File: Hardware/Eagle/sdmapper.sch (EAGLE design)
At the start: 30 parts, among them IC1 AM29F010J, IC2 HM628512ASOP32, IC3 XC95144XL_TQ100, IC4 LM1117-3V3, T1 BC857, T2 BC857

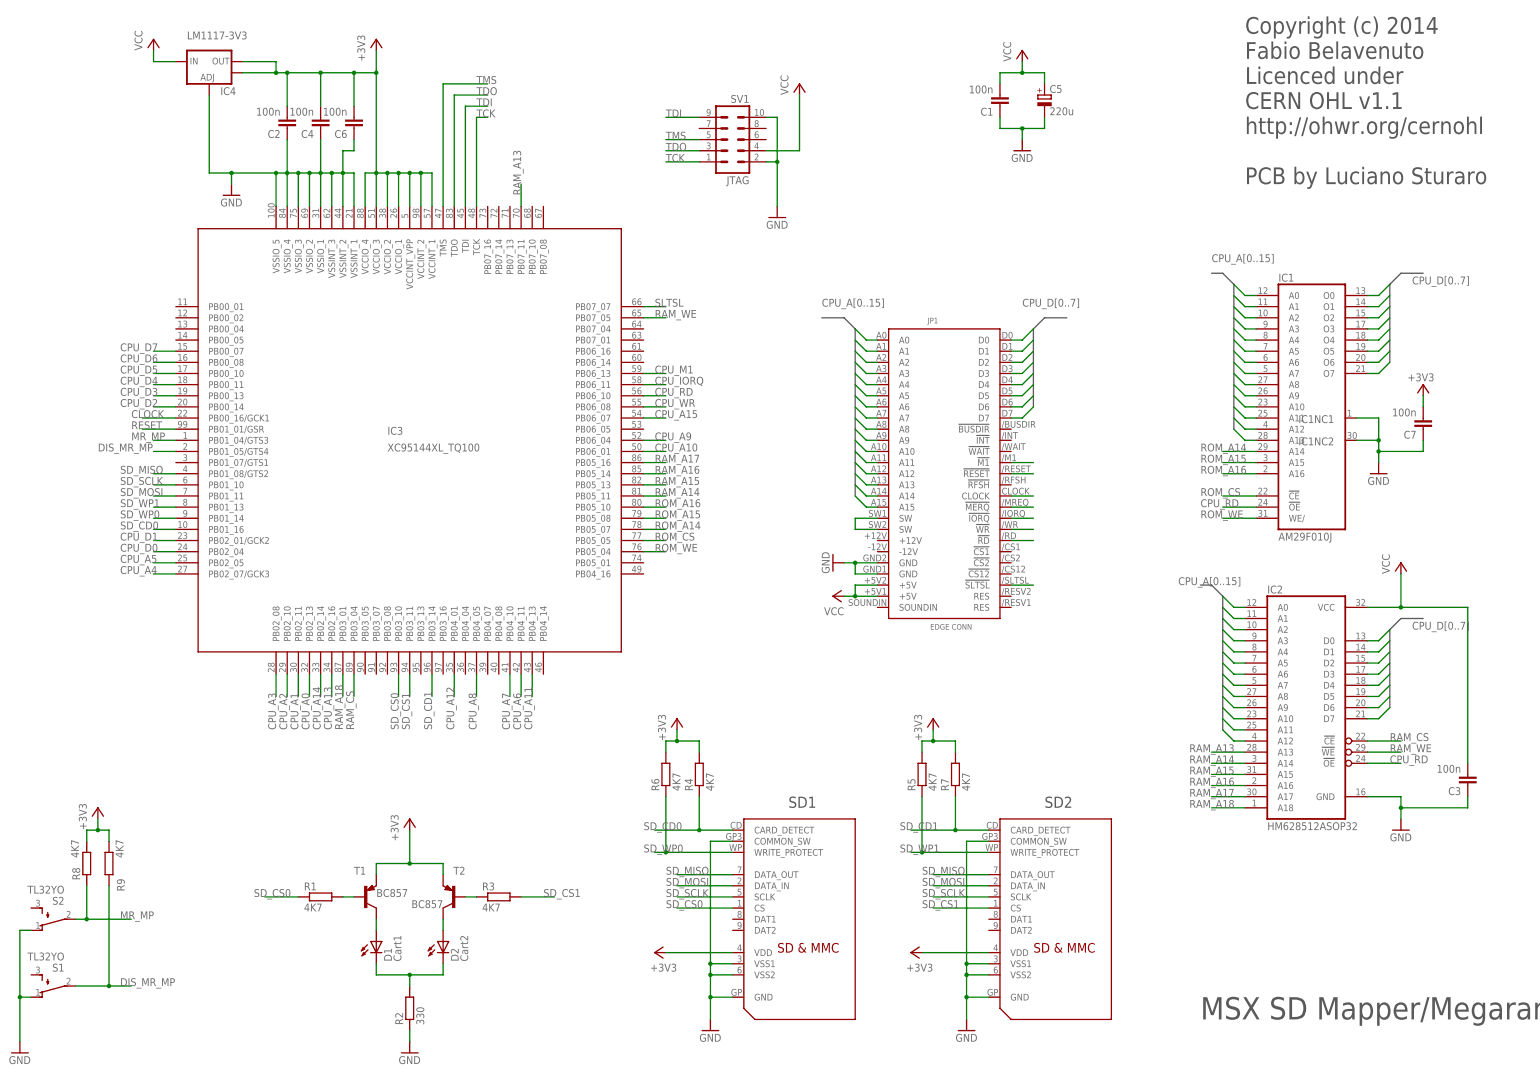
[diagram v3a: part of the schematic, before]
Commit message: CPLD com pinout do produto final. Adicionado versao 2.0.3 do Nextor. Mudado nome da ROM de NEXTOR.ROM para SDMAPPER.ROM Adicionado na inicializacao do driver a chamada a funcao INITXT para exibir mensagens em screen0. Adicionado utilitarios novos.
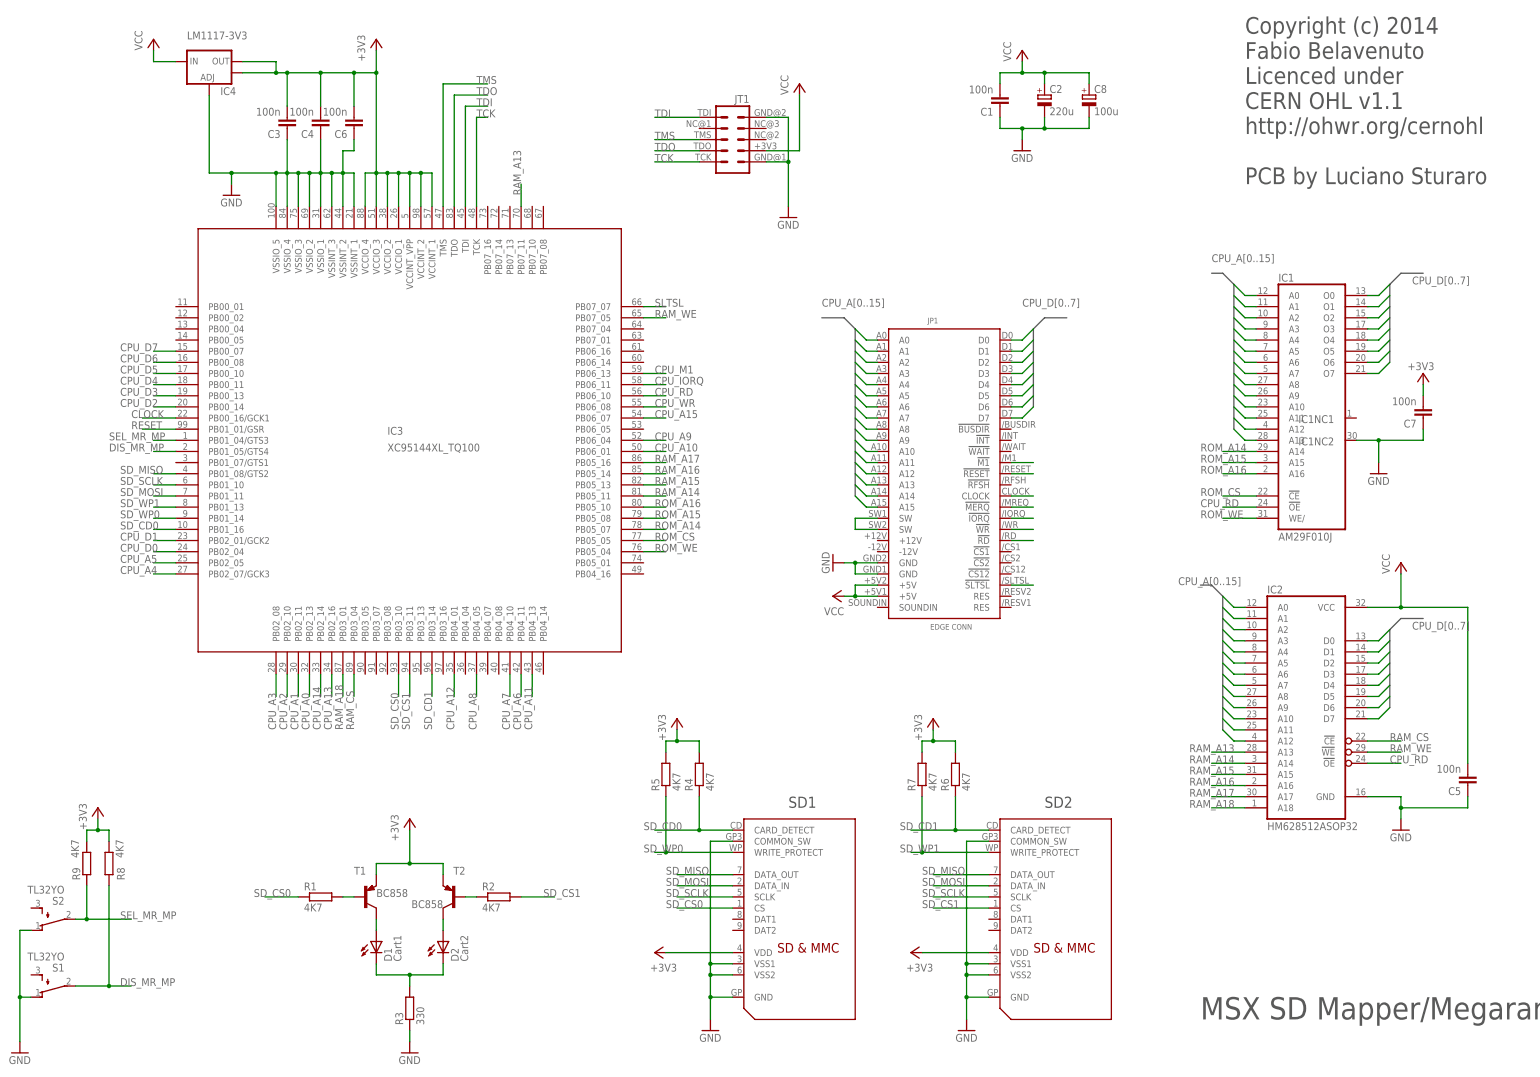
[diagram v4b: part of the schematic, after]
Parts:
- removed SV1: JTAG, con-lstb:MA05-2
- added C8: 100u, rcl:CPOL-EUC
- added JT1: (no value), JTAGs:JTAG1B
- C1, C3, C4: device rcl:C-EUC1206 -> rcl:C-EUC0805
- C2: value 100n -> 220u; device rcl:C-EUC1206 -> rcl:CPOL-EUE3.5-8
- C5: value 220u -> 100n; device rcl:CPOL-EUE2-5 -> rcl:C-EUC0805
- R1, R4, R5, R6, R7, R8, R9: device rcl:R-EU_R1206 -> rcl:R-EU_R0805
- R2: value 330 -> 4K7; device rcl:R-EU_R1206 -> rcl:R-EU_R0805
- R3: value 4K7 -> 330; device rcl:R-EU_R1206 -> rcl:R-EU_R0805
- T1, T2: value BC857 -> BC858; device transistor:BC857C-PNP-SOT23-BEC -> transistor:BC858A-PNP-SOT23-BEC
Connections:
- removed net MR_MP: IC3.PB01_04/GTS3, R8.1, S2.P
- new net SEL_MR_MP: IC3.PB01_04/GTS3, R9.1, S2.P
- net +3V3: now also C3.2; no longer C2.2
- net DIS_MR_MP: now also R8.1; no longer R9.1
- net GND: now also C2.-, C5.1, C8.-, JT1.TCK, JT1.TDI, R3.1; no longer C2.1, C5.-, IC1NC1.NC, R2.1, SV1.10, SV1.2
- net N$5: now also R2.1; no longer R3.1
- net N$7: now also R3.2; no longer R2.2
- net SD_CD1: now also R6.1; no longer R7.1
- net SD_CS1: now also R2.2; no longer R3.2
- net SD_WP0: now also R5.1; no longer R6.1
- net SD_WP1: now also R7.1; no longer R5.1
- net TCK: now also JT1.GND@2; no longer SV1.1
- net TDI: now also JT1.GND@1; no longer SV1.9
- net TDO: now also JT1.NC@3; no longer SV1.3
- net TMS: now also JT1.NC@2; no longer SV1.5
- net VCC: now also C2.+, C5.2, C8.+, JT1.NC@1; no longer C3.2, C5.+, SV1.4
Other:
- moved on the sheet: C3, C7, R2, R3, R5, R6, R7, R8, R9

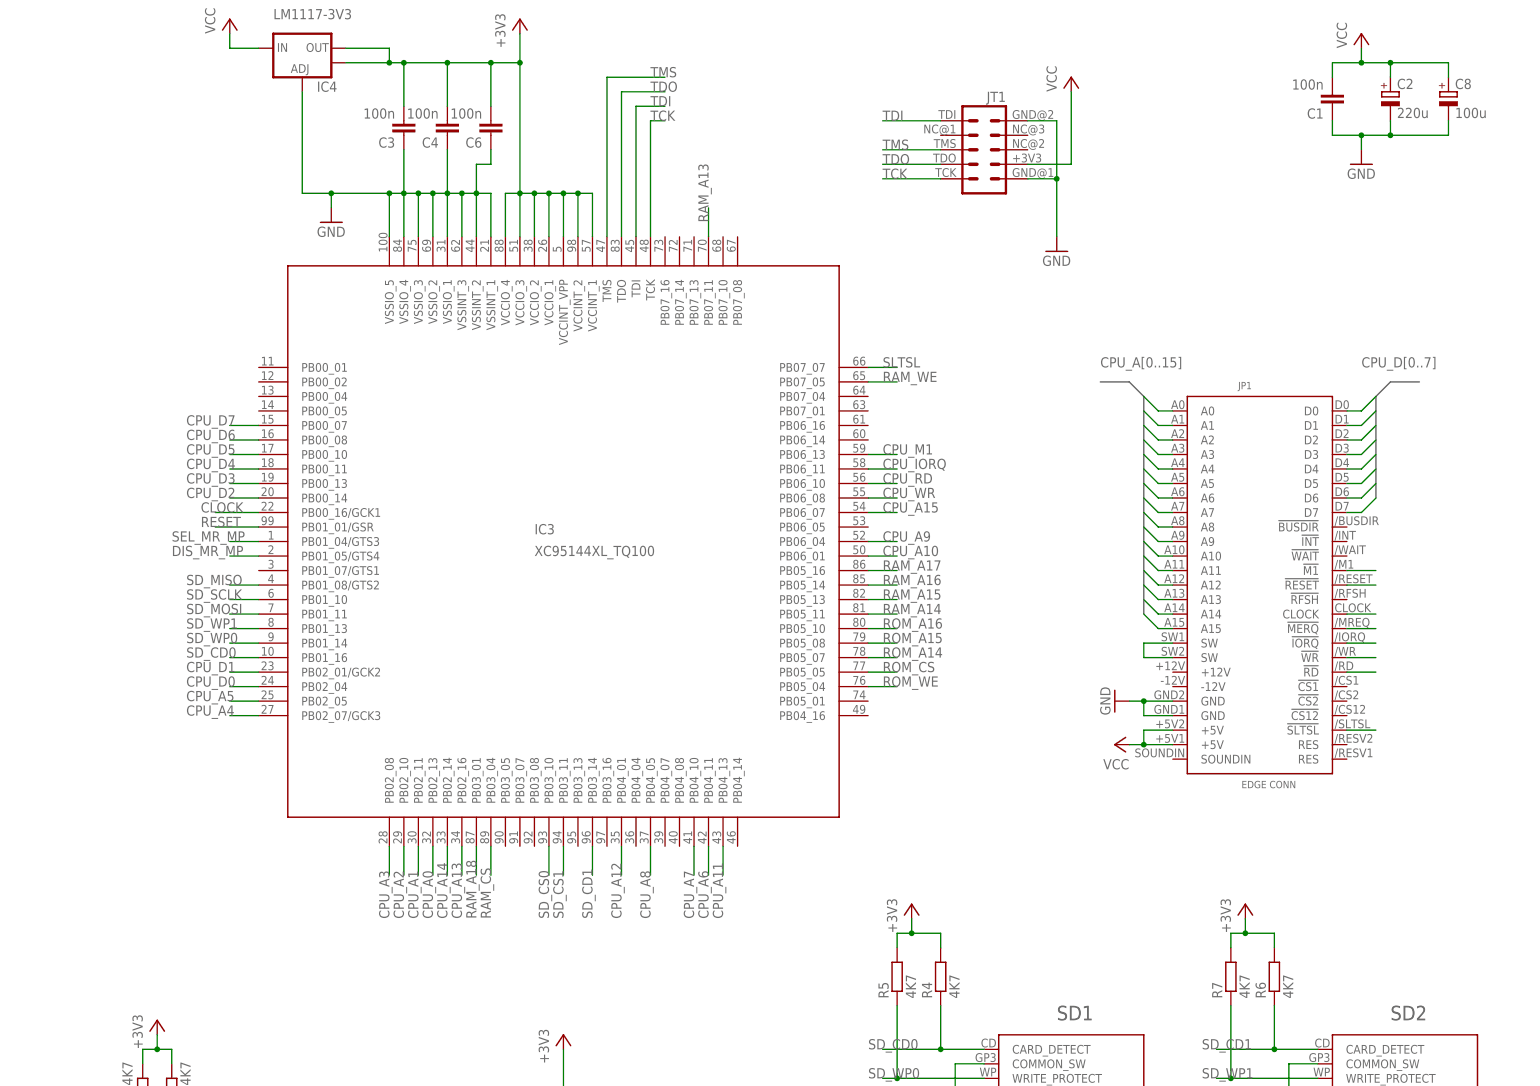
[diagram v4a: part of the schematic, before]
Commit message: Adicionado gerbers da placa roteada pelo Sturaro Adicionado versão em PDF e postscript da placa para fabricação caseira Adicionado lista de materiais Adicionado etiquetas em alta resolução para a caixa final
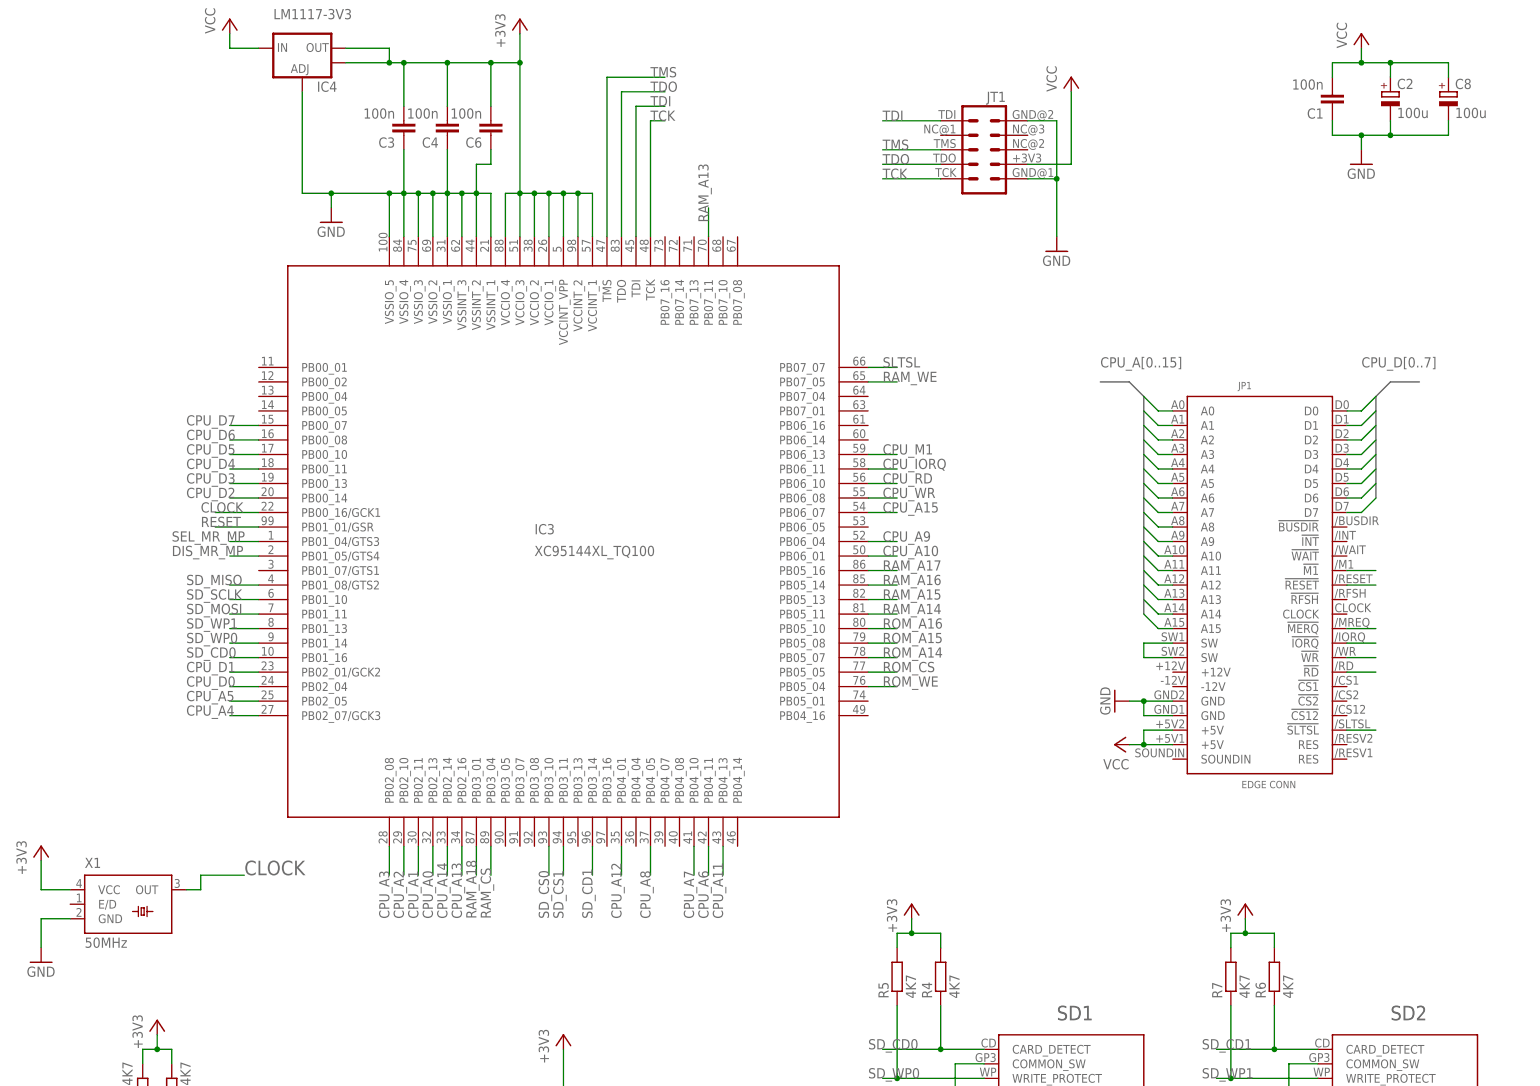
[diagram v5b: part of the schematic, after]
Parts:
- added X1: 50MHz, crystal:SM77H
- C2: value 220u -> 100u
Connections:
- net +3V3: now also X1.VCC
- net CLOCK: now also X1.OUT; no longer JP1.CLOCK
- net GND: now also X1.GND
